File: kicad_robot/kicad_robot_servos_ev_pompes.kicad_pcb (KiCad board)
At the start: 2 copper layers, 99.1 x 61 mm, 66 parts, among them J1 Conn_I2C, J10 Conn_SERVO_3, J11 Conn_SERVO_4, J12 Conn_SERVO_5, J13 Conn_EV_1, J14 Conn_EV_2, J15 Conn_EV_3, J16 Conn_EV_4, J17 Conn_EV_5, J2 Screw_Terminal_POWER, J3 Conn_POMPE_1, J4 Conn_POMPE_5, J5 Conn_POMPE_2, J6 Conn_POMPE_3, J7 Conn_POMPE_4, J8 Conn_SERVO_1, J9 Conn_SERVO_2, Q1 IRLML0030, Q10 IRLML0030, Q2 IRLML0030, Q3 IRLML0030, Q4 IRLML0030, Q5 IRLML0030, Q6 IRLML0030, Q7 IRLML0030, Q8 IRLML0030, Q9 IRLML0030, U1 TSR_1-2450, U2 LM3940, U3 ADC128D818, U4 PCA9685PW, U5 ACS722xLCTR-05AB, U6 ACS722xLCTR-05AB, U7 ACS722xLCTR-05AB, U8 ACS722xLCTR-05AB, U9 ACS722xLCTR-05AB

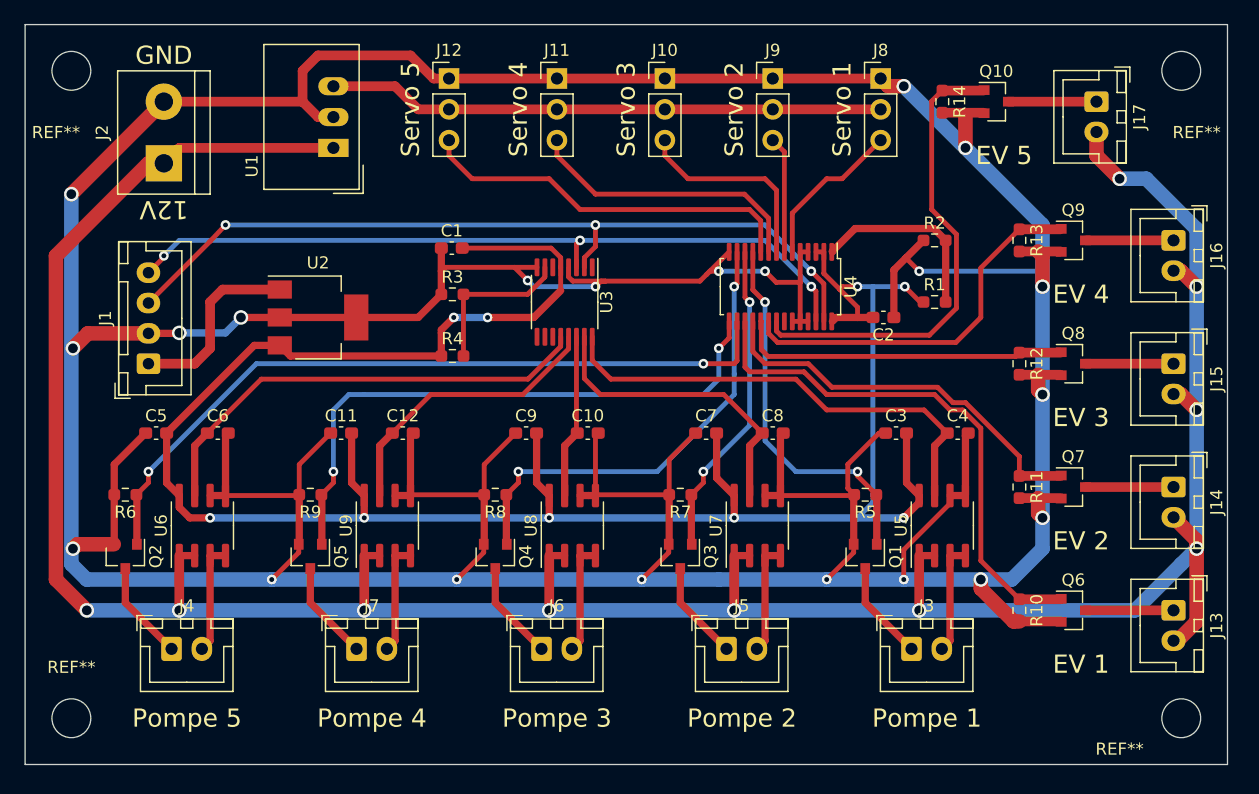
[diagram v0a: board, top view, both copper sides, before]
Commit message: Calage des edge cuts et des mounting holes sur grille 1mm, épaissisement  et décalage tracks
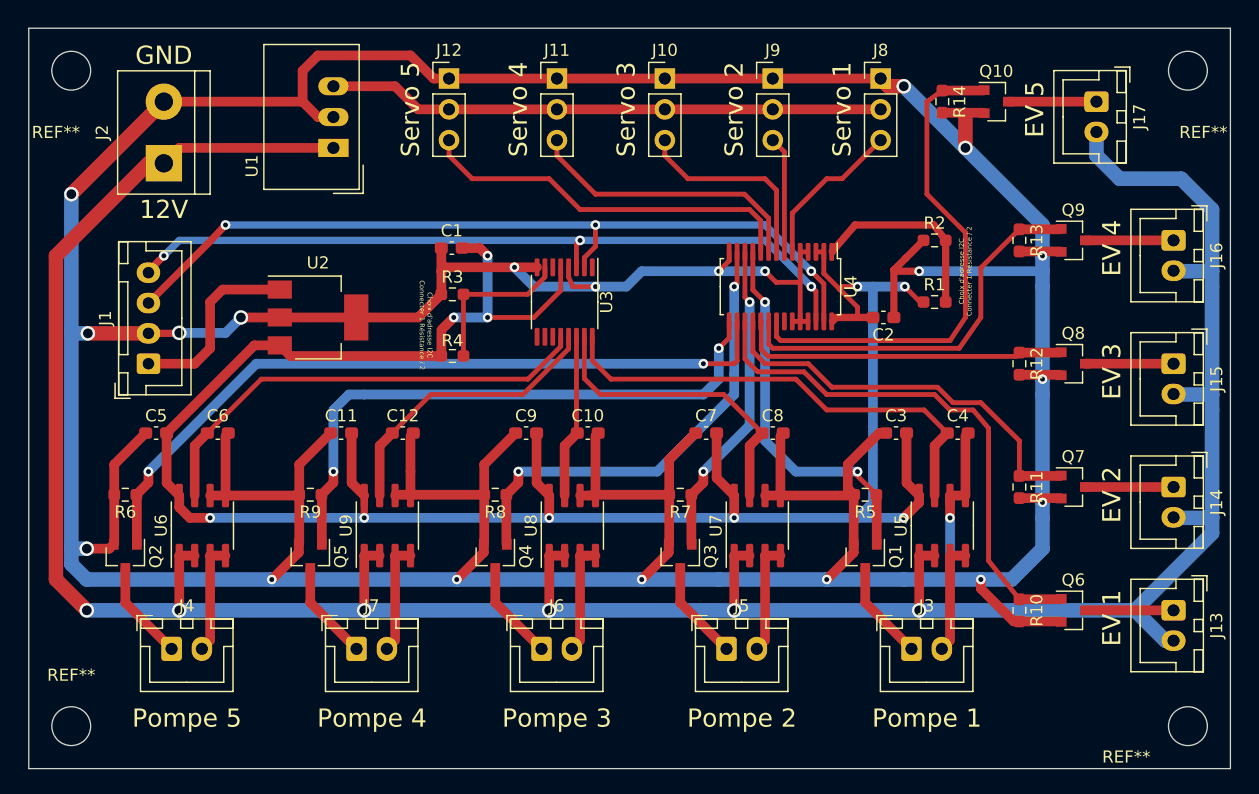
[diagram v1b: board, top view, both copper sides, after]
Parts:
- moved REF** 0.85 mm to (108.5, 70.5)
- moved REF** 0.65 mm to (16.5, 70.5)
- moved REF** 0.55 mm to (108.5, 16.5)
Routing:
- net GND: track 503.9 -> 495.6 mm
- net /EV_5: track 39.3 -> 42.1 mm
- net +3V3: track 185.2 -> 183.4 mm, vias 9 -> 10
- net /EV_4: track 31.7 -> 32.9 mm
- net /EV_2: track 33.1 -> 33.8 mm
- net +12V: vias 10 -> 6
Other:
- board size 99.1 x 61 mm -> 99 x 61 mm
- board text added: "Choix d'adresse I2C Connecter 1 Résistance / 2"

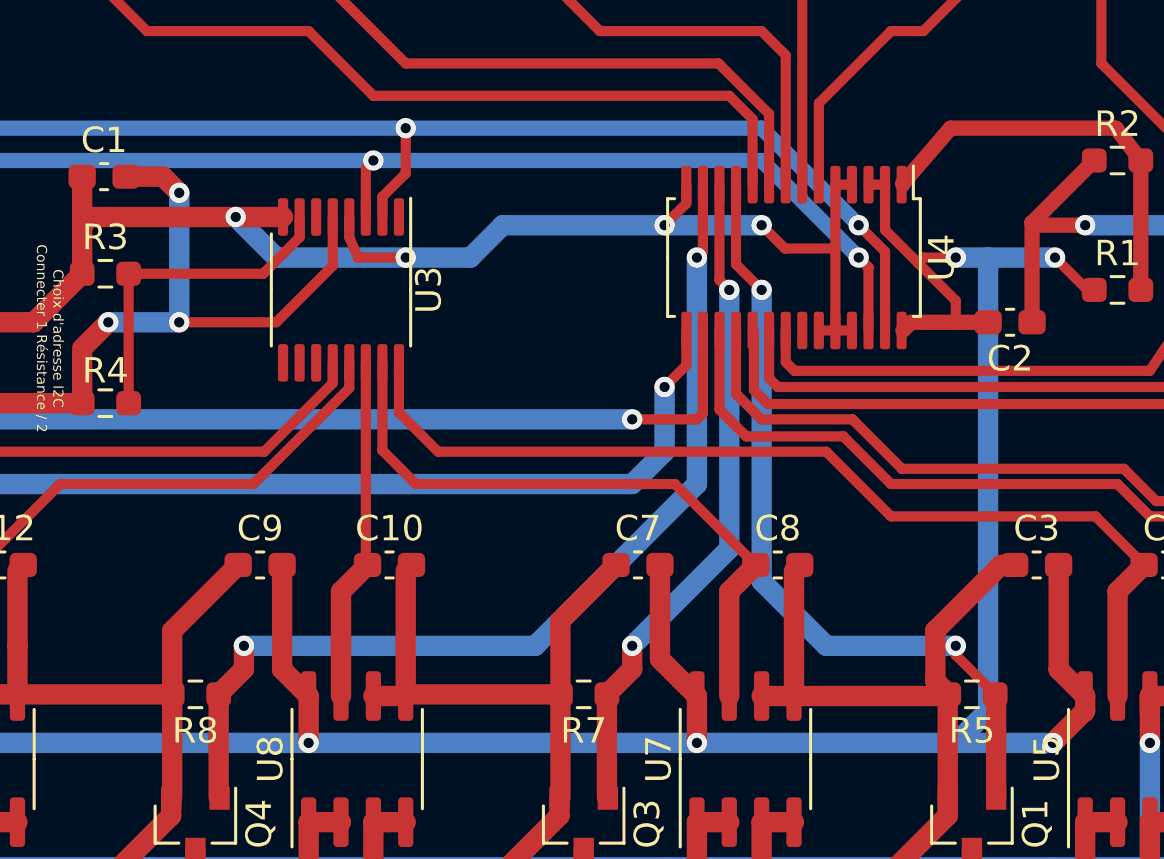
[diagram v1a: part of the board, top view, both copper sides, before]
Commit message: Écartement de vias et pistes encore trop proches
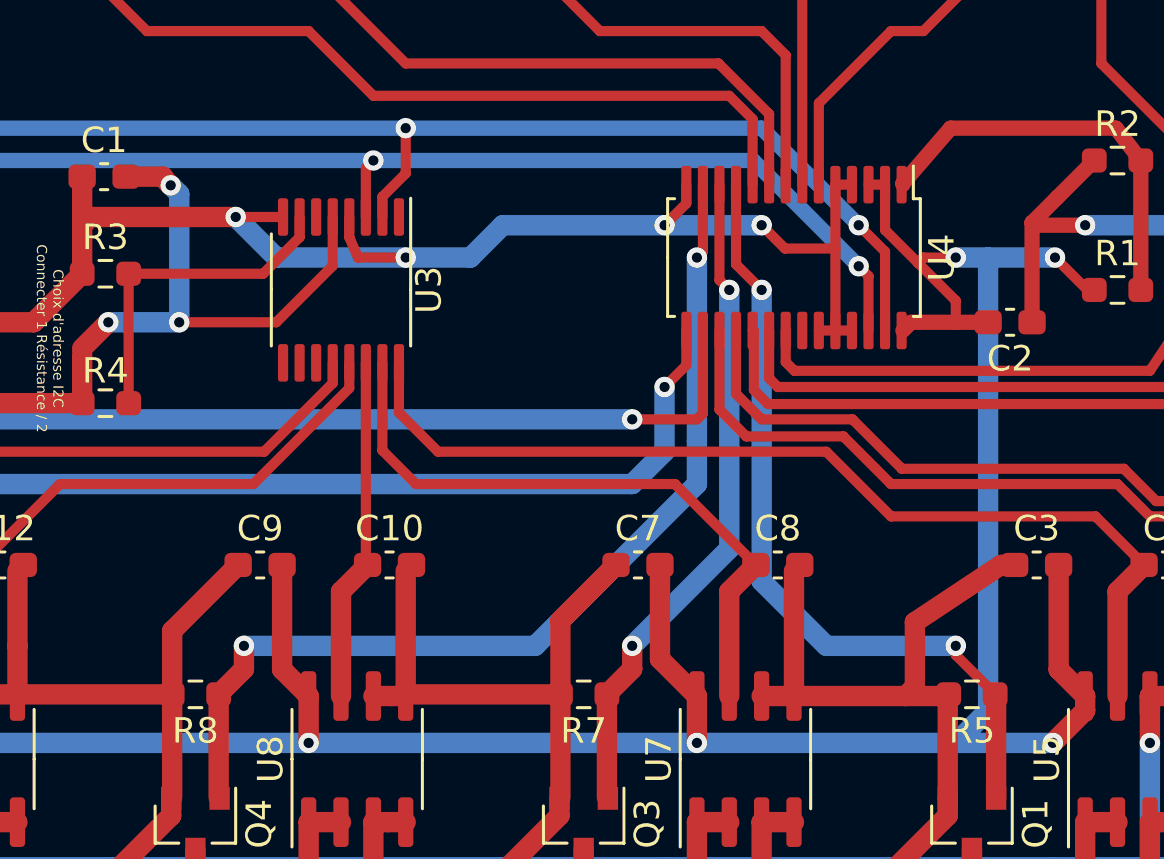
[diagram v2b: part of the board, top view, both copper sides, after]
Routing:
- net GND: track 495.6 -> 496.3 mm

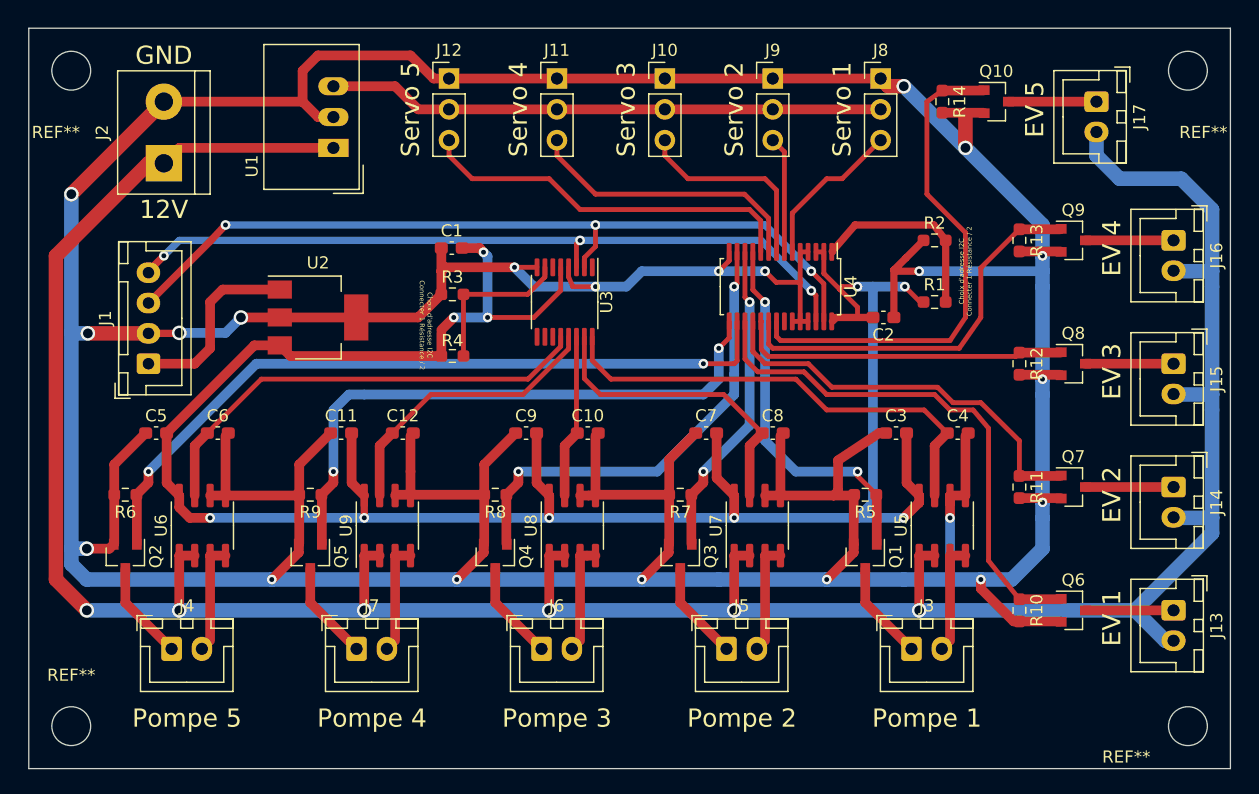
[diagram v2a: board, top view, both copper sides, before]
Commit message: Passage de certaines tracks en bottom, supression de vias inutiles
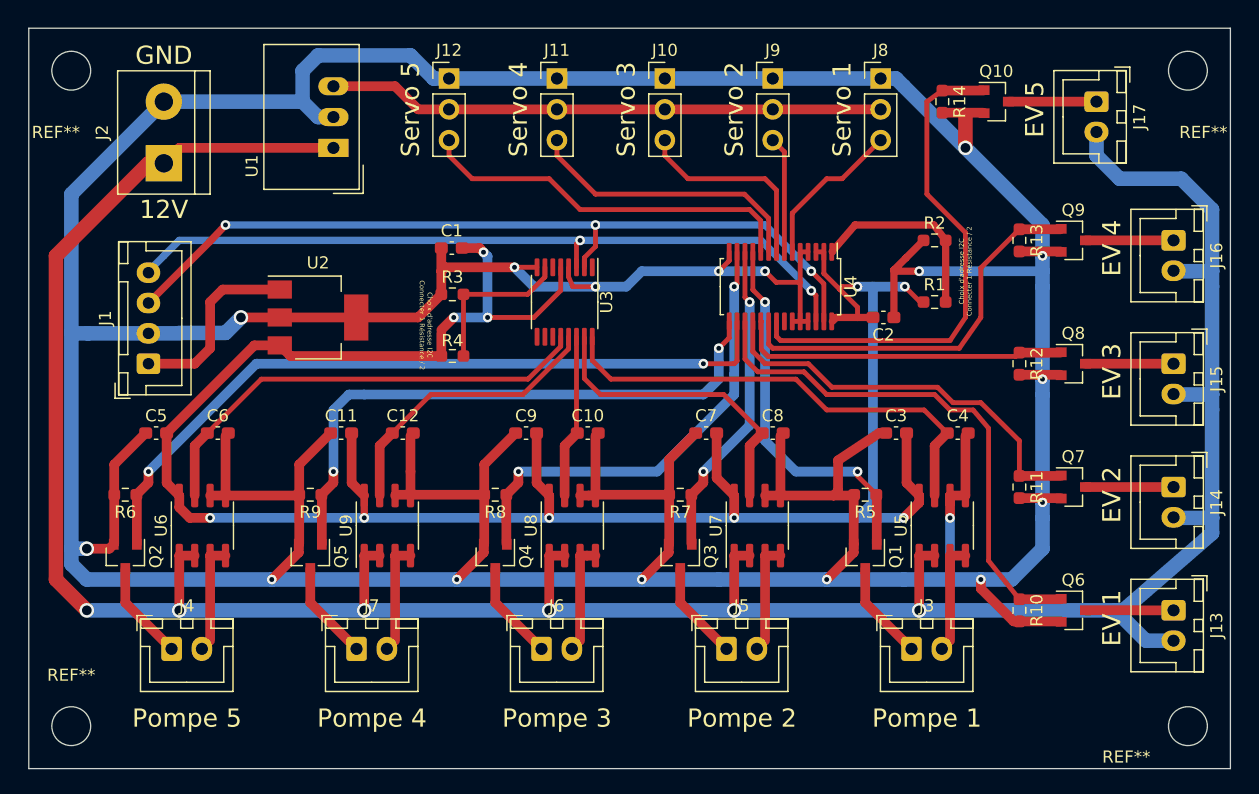
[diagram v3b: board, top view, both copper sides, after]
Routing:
- net +12V: track 235.1 -> 236.5 mm
- net /EXT_SCL: track 62.8 -> 62.7 mm, vias 3 -> 2
- net GND: vias 21 -> 17
